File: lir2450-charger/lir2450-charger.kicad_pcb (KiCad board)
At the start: 2 copper layers, 40.6 x 27.2 mm, 11 parts, among them P1 USB_C_Plug_USB2.0, U1 MCP73831-2-OT

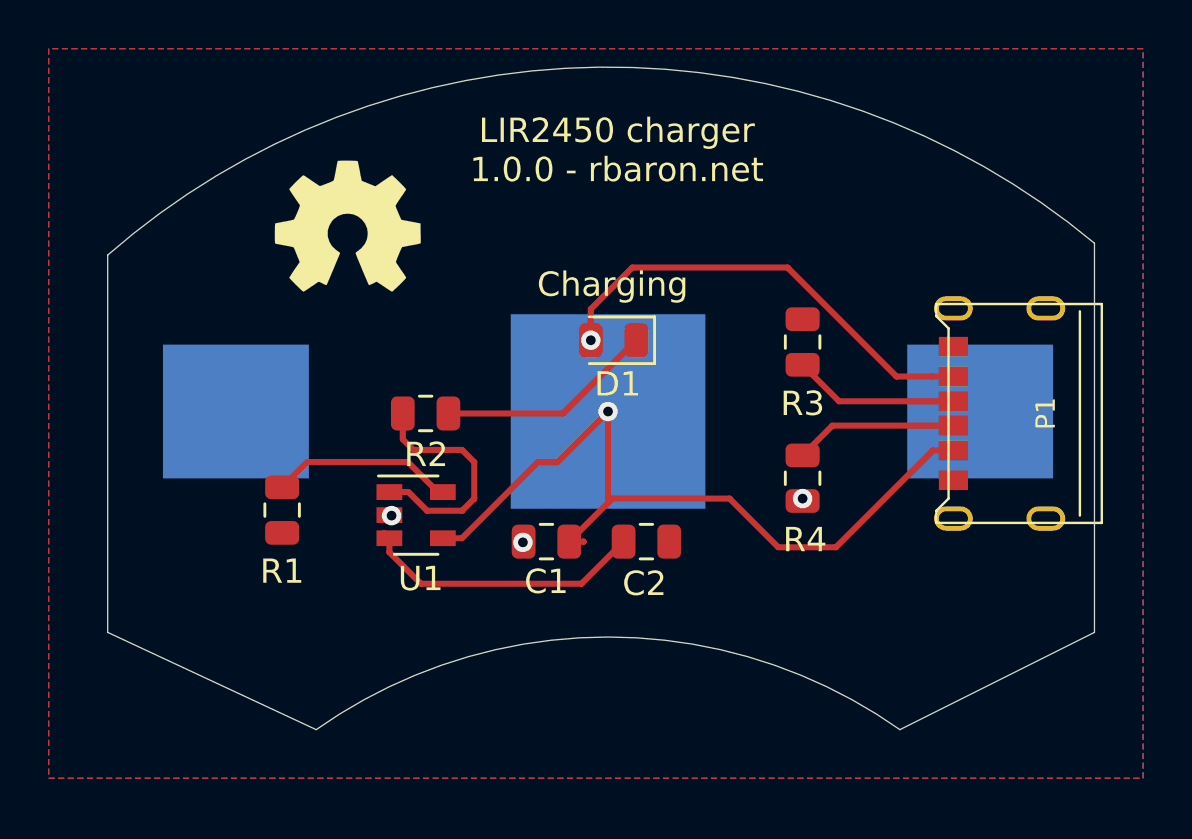
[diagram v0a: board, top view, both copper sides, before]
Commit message: Adds green led & pcb icons
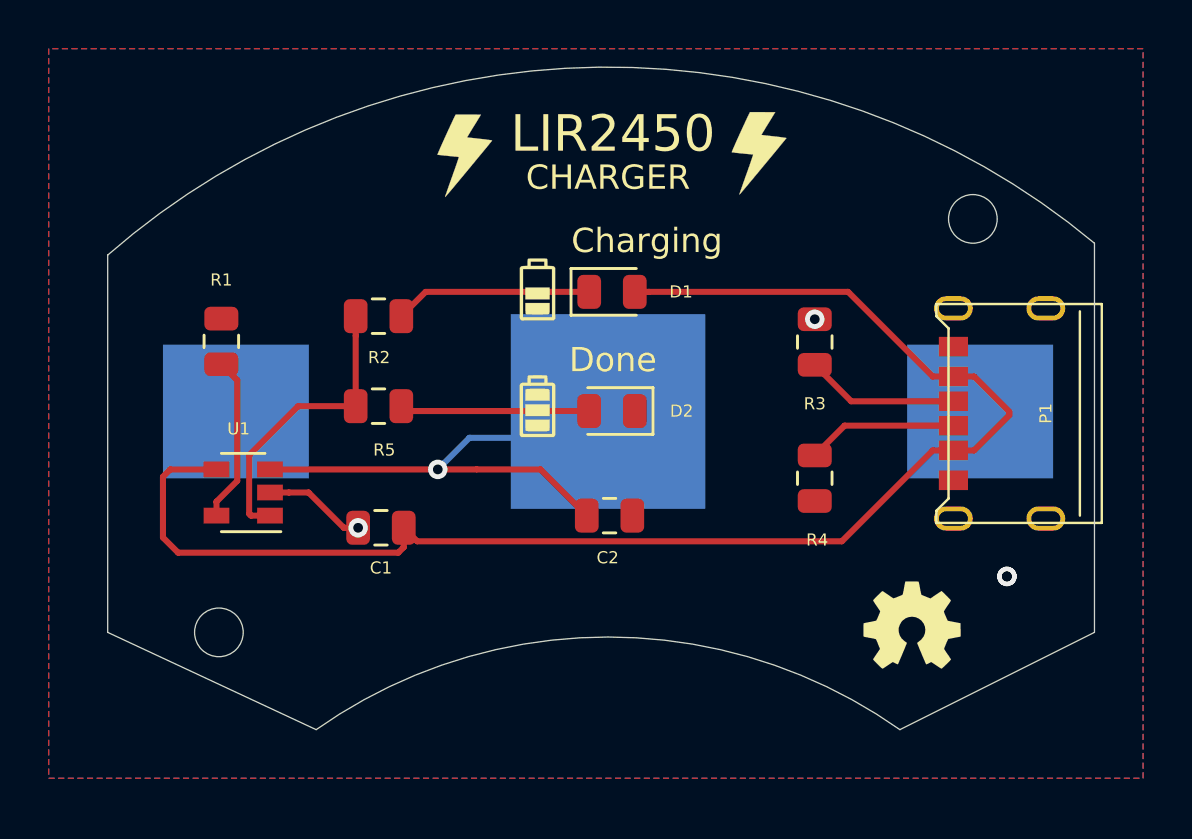
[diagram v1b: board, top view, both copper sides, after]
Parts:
- removed the G*** at (62.3, 37.3)
- added D2: Green LED, LED_SMD:LED_0805_2012Metric, F.Cu at (73.2, 44.9)
- added G***: OSHW-logo_silkscreen-back_4mm, OSHW-logo:OSHW-logo_silkscreen-back_4mm, F.Cu at (85.5, 53.7)
- added G***: LOGO, assets:spark, F.Cu at (79.2, 34.3)
- added G***: LOGO, assets:spark, F.Cu at (67.1, 34.4)
- added G***: LOGO, assets:battery-half, F.Cu at (70.1, 39.9)
- added G***: LOGO, assets:battery-full, F.Cu at (70.1, 44.7)
- added R5: 220, Resistor_SMD:R_0805_2012Metric, F.Cu at (63.6, 44.7)
- D1: value LED -> Red LED
- R2: value 470 -> 220
- moved R1 7.37 mm to (57.1, 42.0), turned to 90 degrees
- moved U1 7.17 mm to (58.0, 48.2), turned to 180 degrees
- moved C1 6.83 mm to (63.7, 49.7)
- moved R2 4.44 mm to (63.6, 41.0)
- moved D1 1.99 mm to (73.2, 40.0), turned to 0 degrees
- moved C2 1.85 mm to (73.1, 49.2)
- moved R3 0.50 mm to (81.5, 42.1)
- moved R4 0.50 mm to (81.5, 47.7)
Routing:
- net Net-(BAT1-PadPos): track 12.0 -> 21.8 mm, vias 0 -> 1
- net +5V: track 51.0 -> 60.7 mm, vias 2 -> 0
- net Net-(D2-Pad2): track 0.00 -> 7.81 mm
- net GND: track 0.00 -> 4.23 mm, vias 3 -> 4
- net Net-(R2-Pad2): track 10.1 -> 12.2 mm
- net Net-(D1-Pad1): track 8.98 -> 8.14 mm
- net Net-(R1-Pad1): track 7.55 -> 6.85 mm
- net Net-(P1-PadB5): track 6.82 -> 6.32 mm
- net Net-(P1-PadA5): track 6.71 -> 6.21 mm
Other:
- outline, holes or cut-outs redrawn
- board text added: "1.0.0 rbaron.net"
- board text added: "CHARGER"
- board text added: "Done"
- board text added: "LIR2450"
- board text added: "LIR2450 ONLY!"
- board text removed: "LIR2450 charger 1.0.0 - rbaron.net"

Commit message: Correct battery clip polarity
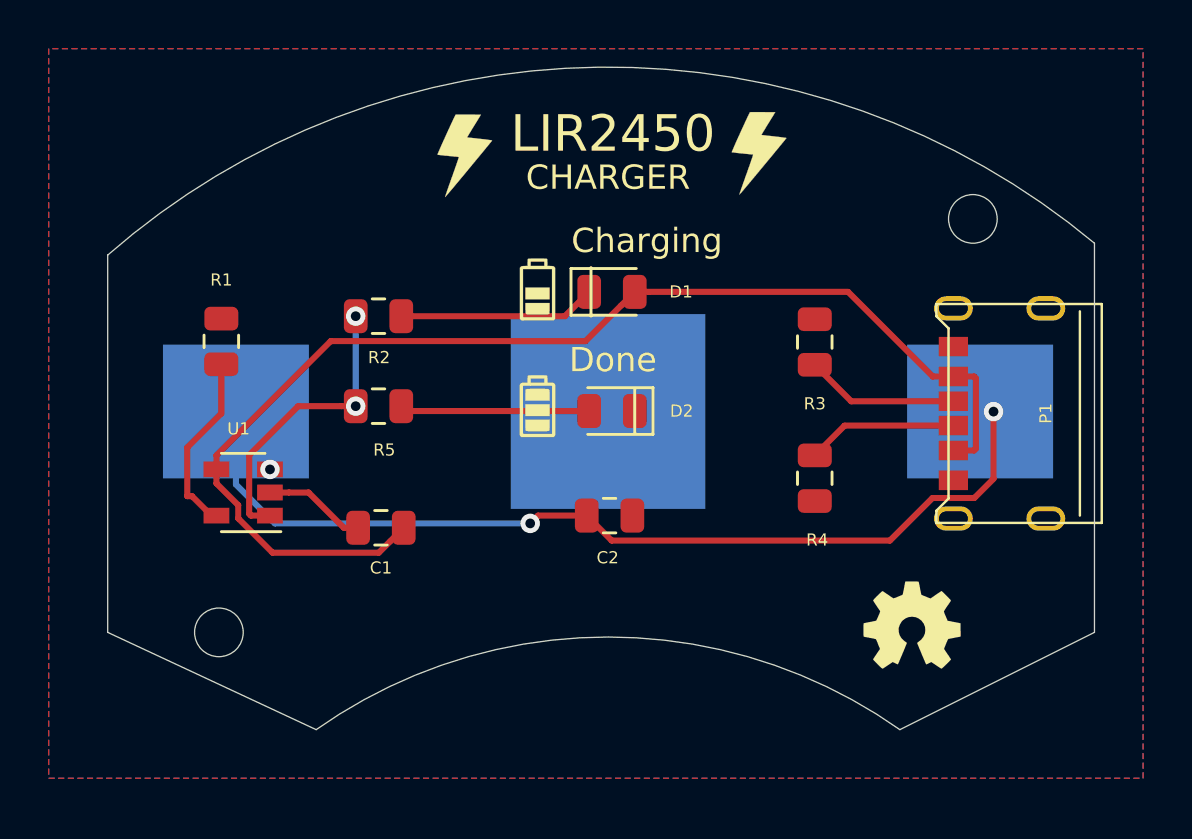
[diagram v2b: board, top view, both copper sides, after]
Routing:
- net Net-(BAT1-PadPos): track 21.8 -> 39.2 mm, vias 1 -> 3
- net +5V: track 60.7 -> 50.1 mm
- net Net-(R1-Pad1): track 6.85 -> 7.54 mm
- net Net-(R2-Pad2): vias 0 -> 2
- net GND: vias 4 -> 0

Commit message: Re-routes some tracks to avoid vias too close to the battery negative pad
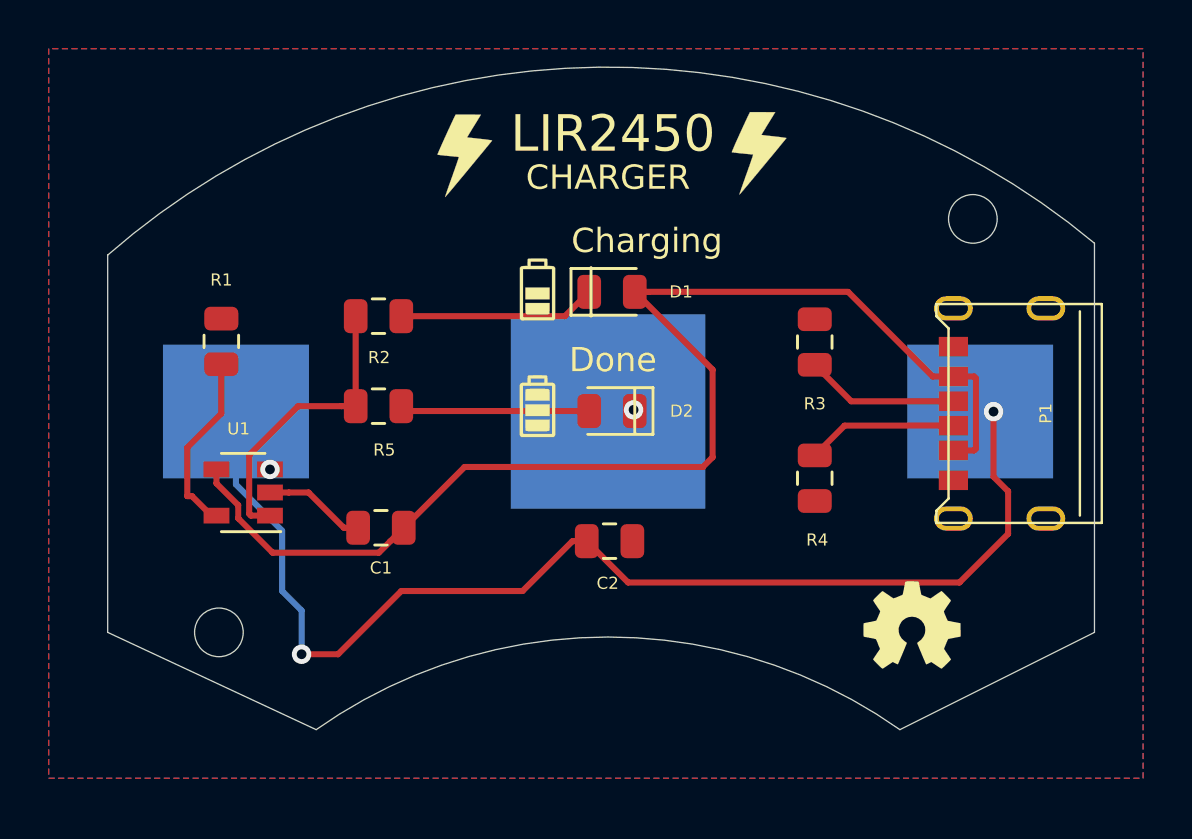
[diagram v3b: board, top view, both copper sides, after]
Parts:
- moved C2 1.05 mm to (73.1, 50.2)
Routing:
- net Net-(BAT1-PadPos): track 39.2 -> 48.9 mm
- net +5V: track 50.1 -> 51.6 mm
- net Net-(R2-Pad2): vias 2 -> 0
- net GND: vias 0 -> 1
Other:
- board text removed: "+"
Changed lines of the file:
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@@
   (general
     (thickness 1.6)
-    (drawings 17)
-    (tracks 62)
+    (drawings 16)
+    (tracks 66)
     (zones 0)
     (modules 17)
@@
       (outputformat 1)
       (mirror false)
-      (drillshape 1)
+      (drillshape 0)
       (scaleselection 1)
-      (outputdirectory ""))
+      (outputdirectory "gerber/"))
   )
   (net 0 "")
@@
   )
   (module Capacitor_SMD:C_0805_2012Metric (layer F.Cu)
-    (at 73.0625 49.2)
+    (at 73.0625 50.25)
     (descr "Capacitor SMD 0805 (2012 Metric), square (rectangular) end terminal, IPC_7351 nominal, (Body size source: https://docs.google.com/spreadsheets/d/1BsfQQcO9C6DZCsRaXUlFlo91Tg2WpOkGARC1WS5S8t0/edit?usp=sharing), generated with kicad-footprint-generator")
     (tags capacitor)
@@
     (effects (font (size 1 1) (thickness 0.15)))
   )
-  (gr_text + (at 66 40.8) (layer B.SilkS)
-    (effects (font (size 3 3) (thickness 0.3)) (justify mirror))
-  )
   (gr_text LIR2450 (at 73.2 33.5) (layer F.SilkS)
     (effects (font (size 1.5 1.5) (thickness 0.2)))
@@
   (gr_arc (start 73 62) (end 92.999999 38.000001) (angle -80.99149626) (layer Edge.Cuts) (width 0.05))
   (gr_line (start 93 38) (end 93 54) (layer Edge.Cuts) (width 0.05))
-  (via (at 69.8 49.520002) (size 0.8) (drill 0.4) (layers F.Cu B.Cu) (net 1))
-  (segment (start 70.120002 49.2) (end 69.8 49.520002) (width 0.25) (layer F.Cu) (net 1))
-  (segment (start 72.125 49.2) (end 70.120002 49.2) (width 0.25) (layer F.Cu) (net 1))
+  (via (at 74.05 44.85) (size 0.8) (drill 0.4) (layers F.Cu B.Cu) (net 2))
+  (via (at 59.1 47.3) (size 0.8) (drill 0.4) (layers F.Cu B.Cu) (net 1))
   (segment (start 57.7 47.919999) (end 57.7 44.92) (width 0.25) (layer B.Cu) (net 1))
-  (segment (start 59.300003 49.520002) (end 57.7 47.919999) (width 0.25) (layer B.Cu) (net 1))
-  (segment (start 69.8 49.520002) (end 59.300003 49.520002) (width 0.25) (layer B.Cu) (net 1))
-  (segment (start 86.339999 48.475001) (end 88.060001 48.475001) (width 0.25) (layer F.Cu) (net 1))
-  (segment (start 72.125 49.2) (end 73.15001 50.22501) (width 0.25) (layer F.Cu) (net 1))
-  (segment (start 84.58999 50.22501) (end 86.339999 48.475001) (width 0.25) (layer F.Cu) (net 1))
+  (segment (start 59.6 49.819999) (end 57.7 47.919999) (width 0.25) (layer B.Cu) (net 1))
+  (segment (start 59.6 52.3) (end 59.6 49.819999) (width 0.25) (layer B.Cu) (net 1))
   (via (at 88.850001 44.92398) (size 0.8) (drill 0.4) (layers F.Cu B.Cu) (net 1))
-  (segment (start 88.850001 47.685001) (end 88.850001 44.92398) (width 0.25) (layer F.Cu) (net 1))
-  (segment (start 88.060001 48.475001) (end 88.850001 47.685001) (width 0.25) (layer F.Cu) (net 1))
-  (segment (start 73.15001 50.22501) (end 84.58999 50.22501) (width 0.25) (layer F.Cu) (net 1))
-  (via (at 59.1 47.3) (size 0.8) (drill 0.4) (layers F.Cu B.Cu) (net 1))
+  (via (at 60.4 54.9) (size 0.8) (drill 0.4) (layers F.Cu B.Cu) (net 1))
+  (segment (start 60.4 53.1) (end 59.6 52.3) (width 0.25) (layer B.Cu) (net 1))
+  (segment (start 60.4 54.9) (end 60.4 53.1) (width 0.25) (layer B.Cu) (net 1))
+  (segment (start 73.825 51.95) (end 72.125 50.25) (width 0.25) (layer F.Cu) (net 1))
+  (segment (start 87.45 51.95) (end 73.825 51.95) (width 0.25) (layer F.Cu) (net 1))
+  (segment (start 89.45 49.95) (end 87.45 51.95) (width 0.25) (layer F.Cu) (net 1))
+  (segment (start 89.45 48.2) (end 89.45 49.95) (width 0.25) (layer F.Cu) (net 1))
+  (segment (start 88.850001 47.600001) (end 89.45 48.2) (width 0.25) (layer F.Cu) (net 1))
+  (segment (start 88.850001 44.92398) (end 88.850001 47.600001) (width 0.25) (layer F.Cu) (net 1))
+  (segment (start 61.9 54.9) (end 60.4 54.9) (width 0.25) (layer F.Cu) (net 1))
+  (segment (start 64.5 52.3) (end 61.9 54.9) (width 0.25) (layer F.Cu) (net 1))
+  (segment (start 69.4875 52.3) (end 64.5 52.3) (width 0.25) (layer F.Cu) (net 1))
+  (segment (start 71.5375 50.25) (end 69.4875 52.3) (width 0.25) (layer F.Cu) (net 1))
+  (segment (start 72.125 50.25) (end 71.5375 50.25) (width 0.25) (layer F.Cu) (net 1))
   (segment (start 59.88 48.25) (end 59.1 48.25) (width 0.25) (layer F.Cu) (net 2))
   (segment (start 60.6875 48.25) (end 59.88 48.25) (width 0.25) (layer F.Cu) (net 2))
@@
   (segment (start 87.2 43.48) (end 86.35 43.48) (width 0.25) (layer F.Cu) (net 3))
   (segment (start 88.05 46.52) (end 87.2 46.52) (width 0.25) (layer F.Cu) (net 3))
-  (segment (start 72.07499 42.02501) (end 73.543763 40.556237) (width 0.25) (layer F.Cu) (net 3))
-  (segment (start 61.59999 42.02501) (end 72.07499 42.02501) (width 0.25) (layer F.Cu) (net 3))
-  (segment (start 56.9 46.725) (end 61.59999 42.02501) (width 0.25) (layer F.Cu) (net 3))
-  (segment (start 73.543763 40.556237) (end 74.1 40) (width 0.25) (layer F.Cu) (net 3))
-  (segment (start 56.9 47.3) (end 56.9 46.725) (width 0.25) (layer F.Cu) (net 3))
-  (segment (start 64.043763 50.256237) (end 64.6 49.7) (width 0.25) (layer F.Cu) (net 3))
-  (segment (start 63.57499 50.72501) (end 64.043763 50.256237) (width 0.25) (layer F.Cu) (net 3))
   (segment (start 59.2086 50.72501) (end 63.57499 50.72501) (width 0.25) (layer F.Cu) (net 3))
-  (segment (start 57.79499 49.3114) (end 59.2086 50.72501) (width 0.25) (layer F.Cu) (net 3))
   (segment (start 57.794989 48.769989) (end 57.79499 49.3114) (width 0.25) (layer F.Cu) (net 3))
   (segment (start 56.9 47.875) (end 57.794989 48.769989) (width 0.25) (layer F.Cu) (net 3))
   (segment (start 56.9 47.3) (end 56.9 47.875) (width 0.25) (layer F.Cu) (net 3))
+  (segment (start 63.57499 50.72501) (end 64.043763 50.256237) (width 0.25) (layer F.Cu) (net 3))
+  (segment (start 64.043763 50.256237) (end 64.6 49.7) (width 0.25) (layer F.Cu) (net 3))
+  (segment (start 57.79499 49.3114) (end 59.2086 50.72501) (width 0.25) (layer F.Cu) (net 3))
+  (segment (start 64.6 49.7) (end 67.1 47.2) (width 0.25) (layer F.Cu) (net 3))
+  (segment (start 67.1 47.2) (end 76.9 47.2) (width 0.25) (layer F.Cu) (net 3))
+  (segment (start 76.9 47.2) (end 77.3 46.8) (width 0.25) (layer F.Cu) (net 3))
+  (segment (start 77.3 43.2) (end 74.1 40) (width 0.25) (layer F.Cu) (net 3))
+  (segment (start 77.3 46.8) (end 77.3 43.2) (width 0.25) (layer F.Cu) (net 3))
   (segment (start 71.225 41) (end 72.225 40) (width 0.25) (layer F.Cu) (net 4))
   (segment (start 64.5 41) (end 71.225 41) (width 0.25) (layer F.Cu) (net 4))
@@
   (segment (start 58.32 49.2) (end 58.244999 49.124999) (width 0.25) (layer F.Cu) (net 8))
   (segment (start 59.1 49.2) (end 58.32 49.2) (width 0.25) (layer F.Cu) (net 8))
-  (via (at 62.625 44.7) (size 0.8) (drill 0.4) (layers F.Cu B.Cu) (net 8))
-  (via (at 62.625 41) (size 0.8) (drill 0.4) (layers F.Cu B.Cu) (net 8))
-  (segment (start 62.625 41) (end 62.625 44.7) (width 0.25) (layer B.Cu) (net 8))
+  (segment (start 62.625 44.7) (end 62.625 41) (width 0.25) (layer F.Cu) (net 8))
   (segment (start 64.7 44.9) (end 64.5 44.7) (width 0.25) (layer F.Cu) (net 9))
   (segment (start 72.225 44.9) (end 64.7 44.9) (width 0.25) (layer F.Cu) (net 9))

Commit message: Adds proper battery footprint
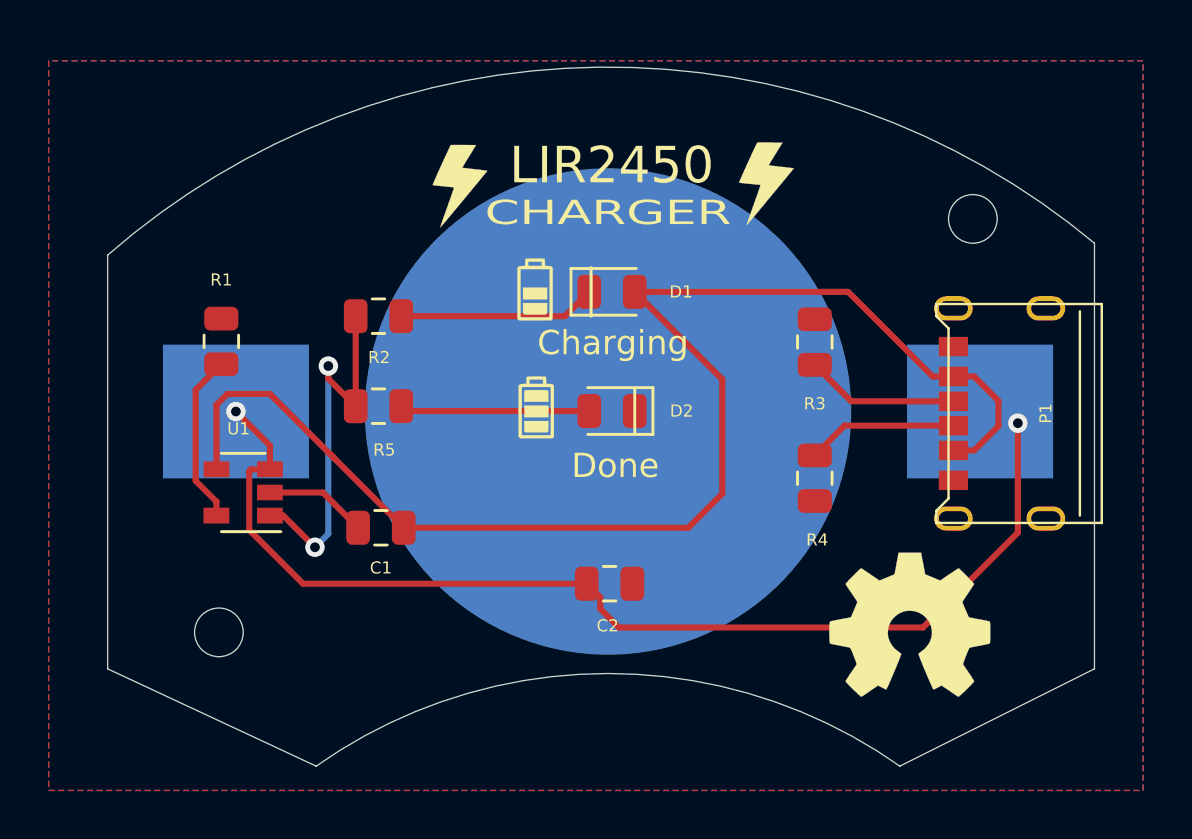
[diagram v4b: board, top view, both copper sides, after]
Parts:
- removed the G*** at (85.5, 53.7)
- removed the G*** at (79.2, 34.3)
- removed the G*** at (67.1, 34.4)
- added G***: LOGO, assets:spark, F.Cu at (79.5, 35.5)
- added G***: LOGO, assets:spark, F.Cu at (66.9, 35.6)
- added REF**: OSHW-Symbol_6.7x6mm_SilkScreen, Symbol:OSHW-Symbol_6.7x6mm_SilkScreen, F.Cu at (85.4, 53.7)
- BAT1: footprint Battery:BatteryHolder_Keystone_3008_1x2450 -> Footprints:BatteryHolder_Keystone_3008_1x2450
- moved C2 1.75 mm to (73.1, 52.0)
- moved G*** 0.10 mm to (70.0, 39.9)
- moved G*** 0.07 mm to (70.0, 44.8)
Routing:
- net +5V: track 51.6 -> 56.7 mm
- net Net-(R2-Pad2): track 12.2 -> 15.9 mm, vias 0 -> 2
- net Net-(BAT1-PadPos): track 48.9 -> 45.9 mm, vias 3 -> 2
- net Net-(R1-Pad1): track 7.54 -> 7.02 mm
- net GND: vias 1 -> 0
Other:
- board size 40.6 x 27.2 mm -> 40.6 x 28.7 mm
- board text removed: "LIR2450 ONLY!"
